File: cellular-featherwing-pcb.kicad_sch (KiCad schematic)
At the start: 65 parts, among them J1 SIM8060-6-0-14-00-A, J2 TSM-116-01-L-SV, J3 TSM-112-01-L-SV, J4 U.FL-R-SMT, U1 BG96, U2 TPS63020QDSJTQ1, U3 TXB0108DQSR, U4 MAX8868EUK30+T

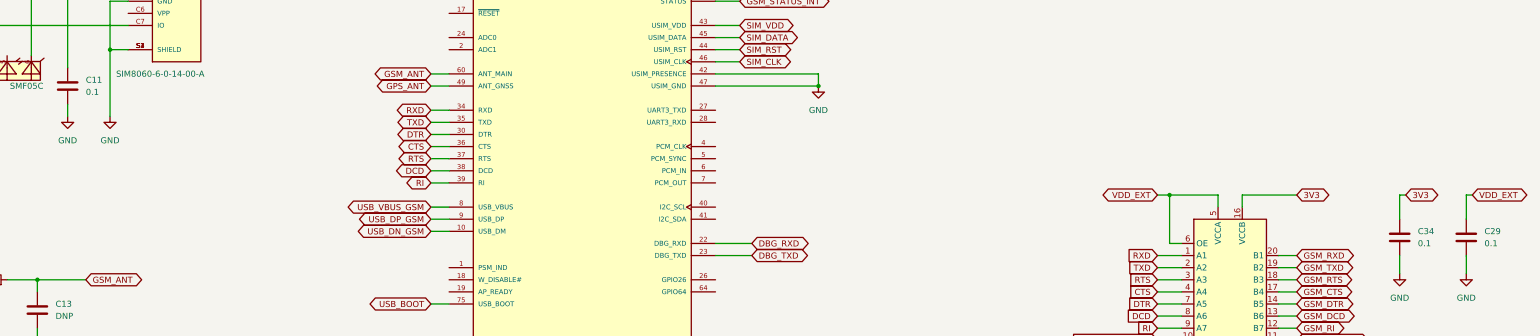
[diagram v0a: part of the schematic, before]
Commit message: Add part numbers and BOM
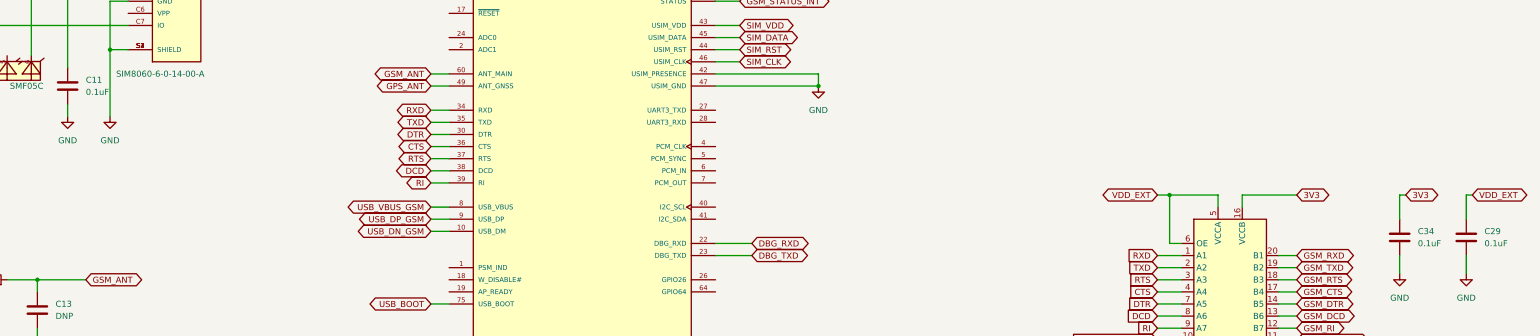
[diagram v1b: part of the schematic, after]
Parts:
- C11, C29, C34: value 0.1 -> 0.1uF; MPN (none) -> CL05B104KO5NNNC
- C16, C17, C18, C22, C23: MPN (none) -> 0402CG330J500NT
- C20, C21, C4: MPN (none) -> CL05B104KO5NNNC
- C24, C25: MPN (none) -> CL05C100JB5NNNC
- C3: MPN (none) -> CL05A225MQ5NSNC
- R1: MPN (none) -> RC0402FR-071M24L
- R14: JLCPCB (none) -> 0402WGF4700TCE; MPN (none) -> 0402WGF4700TCE
- R15: JLCPCB (none) -> 0402WGF1003TCE; MPN (none) -> 0402WGF1003TCE
- R2: MPN (none) -> AC0402FR-07182KL
- R21, R22, R3, R6: MPN RC0402JR-070RP -> 0402WGF0000TCE
- R8: JLCPCB (none) -> 0402WGF1502TCE; MPN (none) -> 0402WGF1502TCE
- U3: Digikey (none) -> https://www.digikey.com/en/products/detail/texas-instrument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
- VT3, VT4: Digikey (none) -> https://www.digikey.com/en/products/detail/rohm-semiconduct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

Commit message: Adding lcsc part numbers for jlpcb
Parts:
- C1, C2, C6, C7, C8: LCSC (none) -> C415703
- C11, C20, C21, C29, C34, C4: LCSC (none) -> C1525
- C13, C9: LCSC (none) -> DNP
- C16, C17, C18, C22, C23: LCSC (none) -> C1562
- C24, C25: LCSC (none) -> C32949
- C26, C28: LCSC (none) -> C347529
- C3: LCSC (none) -> C12530
- C30, C31, C33: LCSC (none) -> C23733
- D1: LCSC (none) -> C85191
- FB1, FB2, FB3, FB4: LCSC (none) -> C15957
- J1: LCSC (none) -> C111371
- J4: LCSC (none) -> C434808
- R1: LCSC (none) -> C166533
- R14: LCSC (none) -> C25117
- R15: LCSC (none) -> C25741
- R2: LCSC (none) -> C226822
- R21, R22, R3, R6: LCSC (none) -> C17168
- R8: LCSC (none) -> C25756
- TP1, TP10, TP11, TP12, TP13, TP14, TP15, TP2, TP8, TP9: LCSC (none) -> DNP; MPN (none) -> DNP
- U1: LCSC (none) -> C3010493
- U2: LCSC (none) -> C202140
- VD1: LCSC (none) -> C316053
- VD4: LCSC (none) -> C72041
- VD5, VD6: LCSC (none) -> C167645
- VT3, VT4: LCSC (none) -> C2971747

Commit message: Files sent to jlpcb
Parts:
- U4: LCSC (none) -> C37970
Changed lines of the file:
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@@
+      (effects (font (size 1.27 1.27)) hide)
+    )
+    (property "LCSC" "C37970" (id 7) (at 240.03 33.02 0)
       (effects (font (size 1.27 1.27)) hide)
     )

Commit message: Updates for jlpcb
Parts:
- removed U3: TXB0108DQSR, Package_SON:USON-20_2x4mm_P0.4mm, symbol Logic_LevelTranslator:TXB0108DQSR
- added U3: TXB0108RGYR, IC_TXB0108RGYR, symbol TXB0108RGYR:TXB0108RGYR
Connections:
- net GSM_DCD_EXT is gone; now on net GSM_DCD: J2.10
- net GSM_RI_EXT is gone; now on net GSM_RI: J3.05
- net 3V3: now also U3.19 (VCCB)
- net CTS: now also U3.5 (A4)
- net DCD: now also U3.7 (A6)
- net DTR: now also U3.6 (A5)
- net GND: now also U3.11 (GND), U3.21 (EXP), U3.21_1 (EXP), U3.21_2 (EXP), U3.21_3 (EXP), U3.21_4 (EXP)
- net GSM_CTS: now also U3.16 (B4)
- net GSM_DCD: now also U3.14 (B6)
- net GSM_DTR: now also U3.15 (B5)
- net GSM_RI: now also U3.13 (B7)
- net GSM_RTS: now also U3.17 (B3)
- net GSM_RXD: now also U3.20 (B1)
- net GSM_STATUS: now also U3.12 (B8)
- net GSM_STATUS_INT: now also U3.9 (A8)
- net GSM_TXD: now also U3.18 (B2)
- net RI: now also U3.8 (A7)
- net RTS: now also U3.4 (A3)
- net RXD: now also U3.1 (A1)
- net TXD: now also U3.3 (A2)
- net VDD_EXT: now also U3.10 (OE), U3.2 (VCCA)
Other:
- moved on the sheet: C29, C34

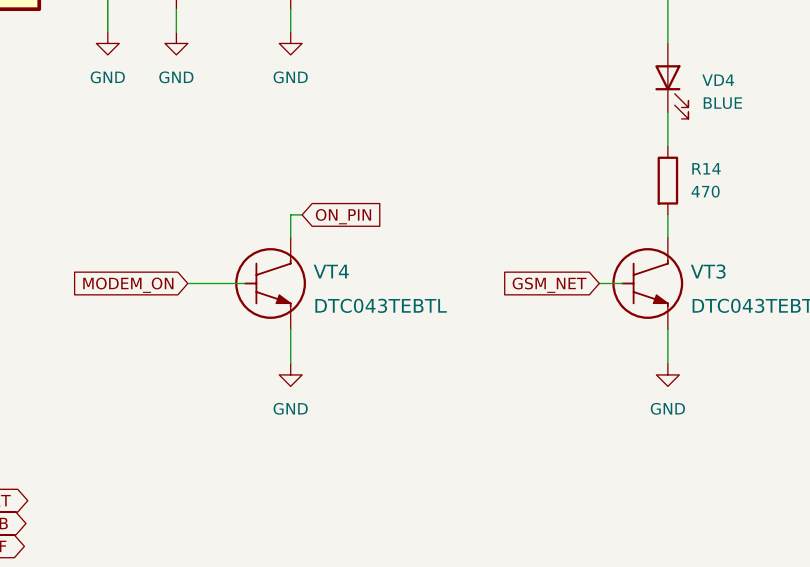
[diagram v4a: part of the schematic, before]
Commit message: #1 Connected LED
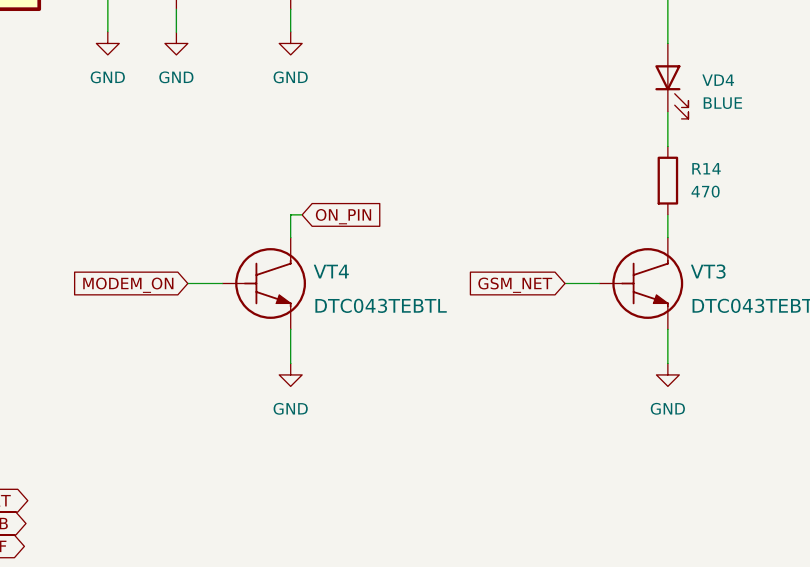
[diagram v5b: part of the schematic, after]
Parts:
- VT3, VT4: footprint ul_DTC043TEBTL:DTC043TEBTL -> TRANS_2SC4617EB_ROM
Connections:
- net GND: now also VT3.2, VT4.2; no longer VT3.3, VT4.3
- net GSM_NET: now also VT3.1
- net MODEM_ON: now also VT4.1
- net ON_PIN: now also VT4.3; no longer VT4.1, VT4.2
- new net: R14.2, VT3.3
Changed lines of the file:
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@@
     (stroke (width 0) (type default) (color 0 0 0 0))
   )
-  (wire (pts (xy 269.24 71.12) (xy 275.59 71.12))
-    (stroke (width 0) (type default) (color 0 0 0 0))
-  )
   (wire (pts (xy 234.95 118.11) (xy 240.03 118.11))
     (stroke (width 0) (type default) (color 0 0 0 0))
@@
     (stroke (width 0) (type default) (color 0 0 0 0))
   )
+  (wire (pts (xy 269.24 71.12) (xy 273.05 71.12))
+    (stroke (width 0) (type default) (color 0 0 0 0))
+  )
   (wire (pts (xy 45.72 21.59) (xy 45.72 31.75))
     (stroke (width 0) (type default) (color 0 0 0 0))
@@
     (stroke (width 0) (type default) (color 0 0 0 0))
   )
-  (wire (pts (xy 314.96 71.12) (xy 317.5 71.12))
-    (stroke (width 0) (type default) (color 0 0 0 0))
-  )
   (wire (pts (xy 299.72 146.05) (xy 304.8 146.05))
     (stroke (width 0) (type default) (color 0 0 0 0))
@@
     (stroke (width 0) (type default) (color 0 0 0 0))
   )
+  (wire (pts (xy 311.15 71.12) (xy 314.96 71.12))
+    (stroke (width 0) (type default) (color 0 0 0 0))
+  )
   (wire (pts (xy 78.74 44.45) (xy 76.2 44.45))
     (stroke (width 0) (type default) (color 0 0 0 0))
@@
     )
   )
-  (global_label "GSM_NET" (shape input) (at 314.96 71.12 180) (fields_autoplaced)
+  (global_label "GSM_NET" (shape input) (at 311.15 71.12 180) (fields_autoplaced)
     (effects (font (size 1.27 1.27)) (justify right))
-    (property "Intersheet References" "${INTERSHEET_REFS}" (id 0) (at 304.2012 71.0406 0)
+    (property "Intersheet References" "${INTERSHEET_REFS}" (id 0) (at 300.3912 71.0406 0)
       (effects (font (size 1.27 1.27)) (justify right) hide)
     )
@@
       (effects (font (size 1.524 1.524)) (justify left))
     )
-    (property "Footprint" "ul_DTC043TEBTL:DTC043TEBTL" (id 2) (at 325.12 77.724 0)
+    (property "Footprint" "TRANS_2SC4617EB_ROM" (id 2) (at 325.12 77.724 0)
       (effects (font (size 1.524 1.524)) hide)
     )
@@
     (pin "2")
   )
-  (symbol (lib_id "dtc043tebtl:DTC043TEBTL") (at 273.05 71.12 0) (unit 1)
+  (symbol (lib_name "DTC043TEBTL_1") (lib_id "dtc043tebtl:DTC043TEBTL") (at 273.05 71.12 0) (unit 1)
     (in_bom yes) (on_board yes) (fields_autoplaced)
     (property "Reference" "VT4" (id 0) (at 283.21 69.85 0)
@@
       (effects (font (size 1.524 1.524)) (justify left))
     )
-    (property "Footprint" "ul_DTC043TEBTL:DTC043TEBTL" (id 2) (at 283.21 77.724 0)
+    (property "Footprint" "TRANS_2SC4617EB_ROM" (id 2) (at 283.21 77.724 0)
       (effects (font (size 1.524 1.524)) hide)
     )
@@
     )
     (path "/1a4c054c-b616-48a3-a8f0-785d2c62e39f"
-      (reference "VT3") (unit 1) (value "DTC043TEBTL") (footprint "ul_DTC043TEBTL:DTC043TEBTL")
+      (reference "VT3") (unit 1) (value "DTC043TEBTL") (footprint "TRANS_2SC4617EB_ROM")
     )
     (path "/43cfd3f4-f7cc-4327-b306-2ed815a7807a"
-      (reference "VT4") (unit 1) (value "DTC043TEBTL") (footprint "ul_DTC043TEBTL:DTC043TEBTL")
+      (reference "VT4") (unit 1) (value "DTC043TEBTL") (footprint "TRANS_2SC4617EB_ROM")
     )
   )

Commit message: Update npn transitor
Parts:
- VT3, VT4: footprint TRANS_2SC4617EB_ROM -> Package_TO_SOT_SMD:SOT-23
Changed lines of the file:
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@@
       (effects (font (size 1.524 1.524)) (justify left))
     )
-    (property "Footprint" "TRANS_2SC4617EB_ROM" (id 2) (at 325.12 77.724 0)
+    (property "Footprint" "Package_TO_SOT_SMD:SOT-23" (id 2) (at 325.12 77.724 0)
       (effects (font (size 1.524 1.524)) hide)
     )
@@
       (effects (font (size 1.524 1.524)) (justify left))
     )
-    (property "Footprint" "TRANS_2SC4617EB_ROM" (id 2) (at 283.21 77.724 0)
+    (property "Footprint" "Package_TO_SOT_SMD:SOT-23" (id 2) (at 283.21 77.724 0)
       (effects (font (size 1.524 1.524)) hide)
     )
@@
     )
     (path "/1a4c054c-b616-48a3-a8f0-785d2c62e39f"
-      (reference "VT3") (unit 1) (value "DTC043TEBTL") (footprint "TRANS_2SC4617EB_ROM")
+      (reference "VT3") (unit 1) (value "DTC043TEBTL") (footprint "Package_TO_SOT_SMD:SOT-23")
     )
     (path "/43cfd3f4-f7cc-4327-b306-2ed815a7807a"
-      (reference "VT4") (unit 1) (value "DTC043TEBTL") (footprint "TRANS_2SC4617EB_ROM")
-    )
-  )
+      (reference "VT4") (unit 1) (value "DTC043TEBTL") (footprint "Package_TO_SOT_SMD:SOT-23")
+    )
+  )
